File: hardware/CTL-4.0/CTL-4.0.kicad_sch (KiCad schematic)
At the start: 67 parts, among them J1 Conn_02x16_Top_Bottom, J3 Conn_01x03, J4 Conn_01x02, J5 Conn_02x06_Odd_Even, J6 Conn_01x04, J7 Conn_01x04, J8 Conn_01x04, K1 G5V-1, Q1 BCX56, Q2 BCX56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

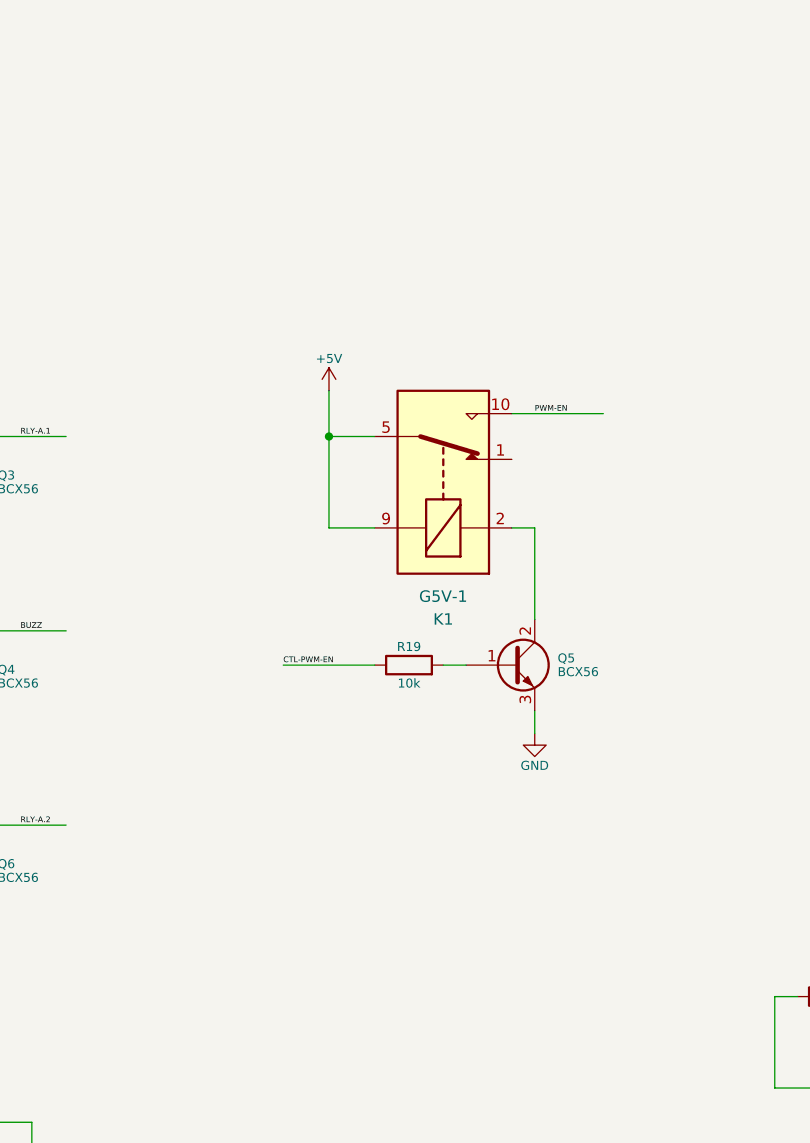
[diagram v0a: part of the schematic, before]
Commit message: modified:   firmware/ESP32-S3 PWM/src/main.cpp 	new file:   hardware/CTL-4.0/CTL-4.0-backups/CTL-4.0-2025-09-30_152410.zip 	new file:   hardware/CTL-4.0/CTL-4.0-backups/CTL-4.0-2025-09-30_153003.zip 	new file:   hardware/CTL-4.0/CTL-4.0-backups/CTL-4.0-2025-09-30_153714.zip 	new file:   hardware/CTL-4.0/CTL-4.0-backups/CTL-4.0-2025-09-30_154923.zip 	new file:   hardware/CTL-4.0/CTL-4.0-backups/CTL-4.0-2025-09-30_155511.zip 	modified:   hardware/CTL-4.0/CTL-4.0.kicad_pcb 	modified:   hardware/CTL-4.0/CTL-4.0.kicad_sch 	modified:   hardware/CTL-4.0/fp-info-cache 	new file:   hardware/CTL-4.1/BoM.xlsx 	new file:   hardware/CTL-4.1/CTL-4.1-backups/CTL-4.1-2025-09-30_155705.zip 	new file:   hardware/CTL-4.1/CTL-4.1-backups/CTL-4.1-2025-09-30_160713.zip 	new file:   hardware/CTL-4.1/CTL-4.1-backups/CTL-4.1-2025-09-30_161258.zip 	new file:   hardware/CTL-4.1/CTL-4.1-backups/CTL-4.1-2025-09-30_161801.zip 	new file:   hardware/CTL-4.1/CTL-4.1-backups/CTL-4.1-2025-09-30_162354.zip 	new file:   hardware/CTL-4.1/CTL-4.1-backups/CTL-4.1-2025-09-30_163220.zip 	new file:   hardware/CTL-4.1/CTL-4.1.FCStd 	new file:   hardware/CTL-4.1/CTL-4.1.iges 	new file:   hardware/CTL-4.1/CTL-4.1.kicad_pcb 	new file:   hardware/CTL-4.1/CTL-4.1.kicad_prl 	new file:   hardware/CTL-4.1/CTL-4.1.kicad_pro 	new file:   hardware/CTL-4.1/CTL-4.1.kicad_sch 	new file:   hardware/CTL-4.1/CTL-4.1.png 	new file:   hardware/CTL-4.1/CTL-4.1.step 	new file:   hardware/CTL-4.1/fp-info-cache
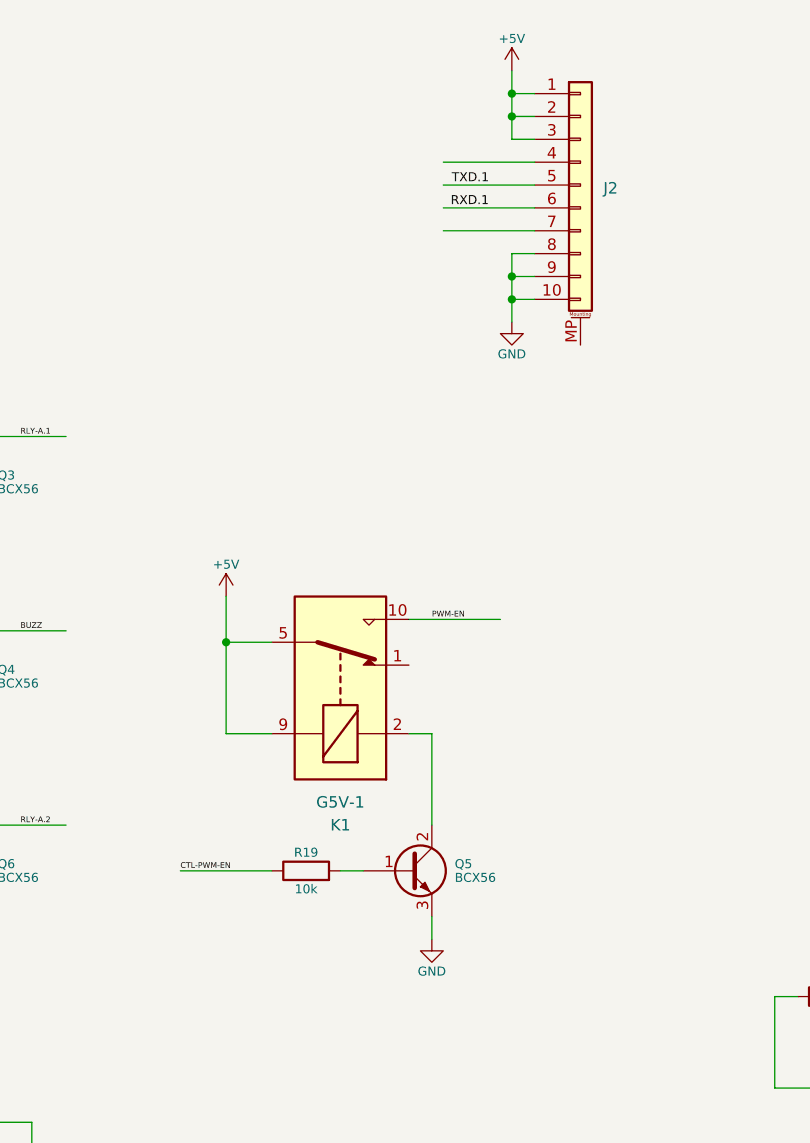
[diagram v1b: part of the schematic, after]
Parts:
- added J2: ~, Connector_FFC-FPC:TE_1-84952-0_1x10-1MP_P1.0mm_Horizontal, symbol Connector_Generic_MountingPin:Conn_01x10_MountingPin
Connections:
- net +5V: now also J2.1 (Pin_1), J2.2 (Pin_2), J2.3 (Pin_3)
- net GND: now also J2.10 (Pin_10), J2.8 (Pin_8), J2.9 (Pin_9)
- net RXD.1: now also J2.6 (Pin_6)
- net TXD.1: now also J2.5 (Pin_5)
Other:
- moved on the sheet: K1, Q5, R19
